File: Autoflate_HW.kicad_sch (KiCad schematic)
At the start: 70 parts, among them J1 JST_XH_3, J10 JST_VH_2, J11 JST_VH_2, J12 JST_XH_3, J13 Header_1, J2 JST_VH_3, J3 JST_XH_2, J4 JST_XH_2, J5 JST_XH_2, J6 JST_XH_2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

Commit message: Added Cap on pressure sensor supply
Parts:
- added C10: 1uF, Capacitor_SMD:C_1206_3216Metric_Pad1.33x1.80mm_HandSolder, symbol Device:C
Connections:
- net +5V: now also C10.1
- net GND: now also C10.2
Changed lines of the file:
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@@
   (junction (at 140.97 38.1) (diameter 0) (color 0 0 0 0)
+  )
+  (junction (at 45.72 146.05) (diameter 0) (color 0 0 0 0)
   )
   (junction (at 99.06 52.07) (diameter 0) (color 0 0 0 0)
@@
     (stroke (width 0) (type default) (color 0 0 0 0))
   )
+  (wire (pts (xy 45.72 146.05) (xy 45.72 144.78))
+    (stroke (width 0) (type default) (color 0 0 0 0))
+  )
   (wire (pts (xy 87.63 72.39) (xy 81.28 72.39))
     (stroke (width 0) (type default) (color 0 0 0 0))
@@
     (stroke (width 0) (type default) (color 0 0 0 0))
   )
-  (wire (pts (xy 45.72 156.21) (xy 45.72 154.94))
+  (wire (pts (xy 45.72 156.21) (xy 45.72 146.05))
     (stroke (width 0) (type default) (color 0 0 0 0))
   )
@@
   )
   (wire (pts (xy 87.63 54.61) (xy 81.28 54.61))
+    (stroke (width 0) (type default) (color 0 0 0 0))
+  )
+  (wire (pts (xy 45.72 146.05) (xy 54.61 146.05))
     (stroke (width 0) (type default) (color 0 0 0 0))
   )
@@
     )
   )
-  (symbol (lib_id "power:+5V") (at 45.72 154.94 0) (unit 1)
-    (in_bom yes) (on_board yes) (fields_autoplaced)
-    (property "Reference" "#PWR0105" (id 0) (at 45.72 158.75 0)
-      (effects (font (size 1.27 1.27)) hide)
-    )
-    (property "Value" "+5V" (id 1) (at 45.72 151.3642 0))
-    (property "Footprint" "" (id 2) (at 45.72 154.94 0)
-      (effects (font (size 1.27 1.27)) hide)
-    )
-    (property "Datasheet" "" (id 3) (at 45.72 154.94 0)
+  (symbol (lib_id "power:+5V") (at 45.72 144.78 0) (unit 1)
+    (in_bom yes) (on_board yes) (fields_autoplaced)
+    (property "Reference" "#PWR0105" (id 0) (at 45.72 148.59 0)
+      (effects (font (size 1.27 1.27)) hide)
+    )
+    (property "Value" "+5V" (id 1) (at 45.72 141.2042 0))
+    (property "Footprint" "" (id 2) (at 45.72 144.78 0)
+      (effects (font (size 1.27 1.27)) hide)
+    )
+    (property "Datasheet" "" (id 3) (at 45.72 144.78 0)
       (effects (font (size 1.27 1.27)) hide)
     )
@@
     (pin "2")
   )
+  (symbol (lib_id "power:GND") (at 54.61 153.67 0) (unit 1)
+    (in_bom yes) (on_board yes)
+    (property "Reference" "#PWR0126" (id 0) (at 54.61 160.02 0)
+      (effects (font (size 1.27 1.27)) hide)
+    )
+    (property "Value" "GND" (id 1) (at 58.42 156.21 0))
+    (property "Footprint" "" (id 2) (at 54.61 153.67 0)
+      (effects (font (size 1.27 1.27)) hide)
+    )
+    (property "Datasheet" "" (id 3) (at 54.61 153.67 0)
+      (effects (font (size 1.27 1.27)) hide)
+    )
+    (pin "1")
+  )
   (symbol (lib_id "Device:C_Polarized_US") (at 125.73 44.45 0) (unit 1)
     (in_bom yes) (on_board yes)
@@
     )
     (pin "1")
+  )
+  (symbol (lib_id "Device:C") (at 54.61 149.86 0) (unit 1)
+    (in_bom yes) (on_board yes) (fields_autoplaced)
+    (property "Reference" "C10" (id 0) (at 57.531 149.0253 0)
+      (effects (font (size 1.27 1.27)) (justify left))
+    )
+    (property "Value" "1uF" (id 1) (at 57.531 151.5622 0)
+      (effects (font (size 1.27 1.27)) (justify left))
+    )
+    (property "Footprint" "Capacitor_SMD:C_1206_3216Metric_Pad1.33x1.80mm_HandSolder" (id 2) (at 55.5752 153.67 0)
+      (effects (font (size 1.27 1.27)) hide)
+    )
+    (property "Datasheet" "~" (id 3) (at 54.61 149.86 0)
+      (effects (font (size 1.27 1.27)) hide)
+    )
+    (pin "1")
+    (pin "2")
   )
   (symbol (lib_id "Device:R") (at 229.87 143.51 90) (unit 1)
@@
       (reference "#PWR0125") (unit 1) (value "GND") (footprint "")
     )
+    (path "/a5583439-f3ce-4044-aa4b-15691ff6bcfb"
+      (reference "#PWR0126") (unit 1) (value "GND") (footprint "")
+    )
     (path "/f71d0b0a-699b-470e-8193-907f94f21c11"
       (reference "#PWR0127") (unit 1) (value "GND") (footprint "")
@@
       (reference "C9") (unit 1) (value "33nF") (footprint "Capacitor_SMD:C_0805_2012Metric_Pad1.18x1.45mm_HandSolder")
     )
+    (path "/e028d976-3098-4bd8-8eba-3e1cb9bf2392"
+      (reference "C10") (unit 1) (value "1uF") (footprint "Capacitor_SMD:C_1206_3216Metric_Pad1.33x1.80mm_HandSolder")
+    )
     (path "/23dcefda-c203-49e7-ab3b-d4962ddc6374"

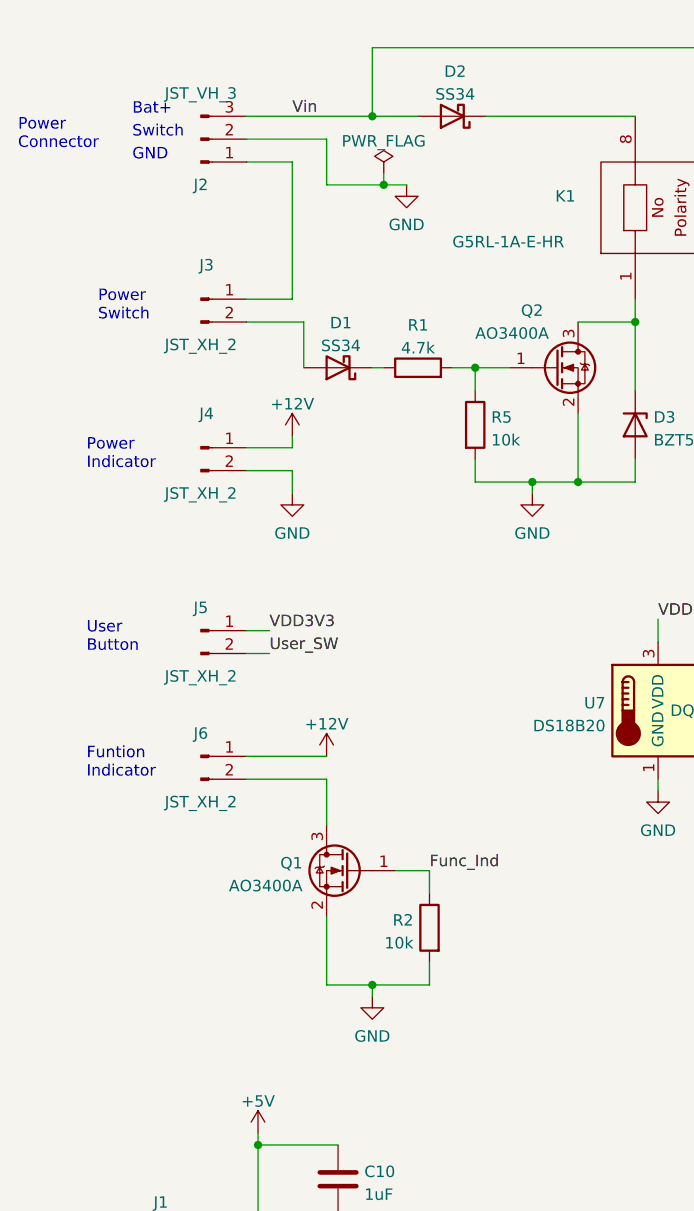
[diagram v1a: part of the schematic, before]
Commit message: 4 pin xh
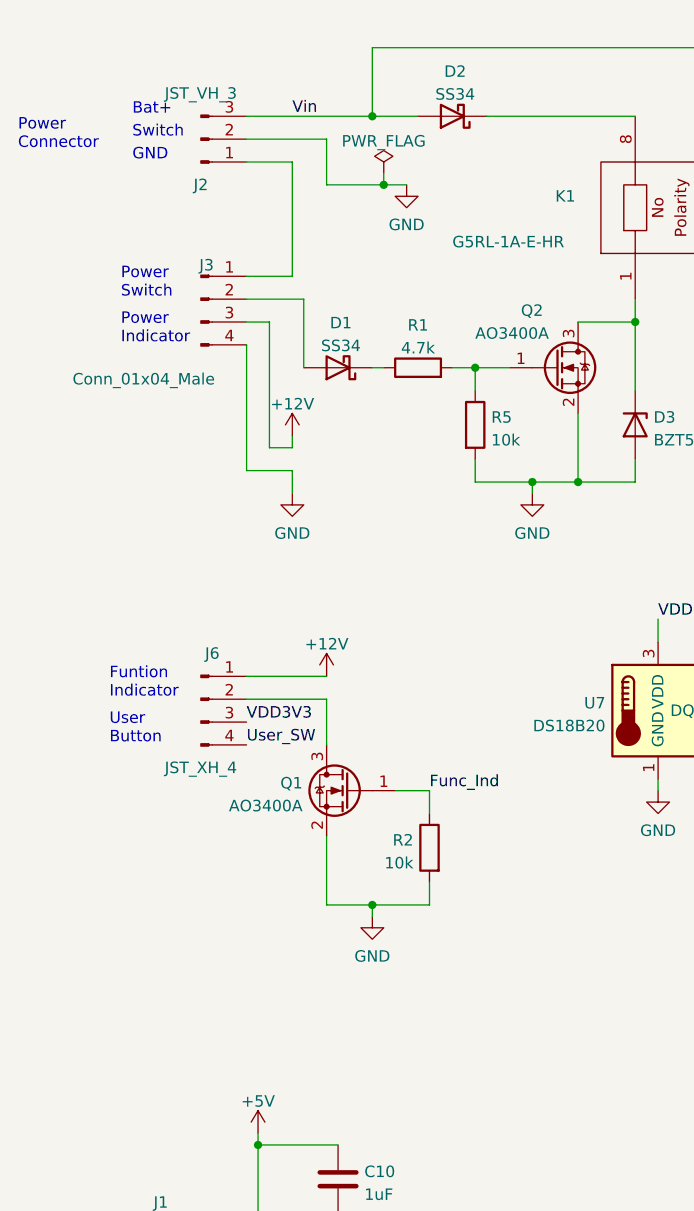
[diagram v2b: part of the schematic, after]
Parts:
- removed J4, J5: JST_XH_2, Connector_JST:JST_XH_B2B-XH-A_1x02_P2.50mm_Vertical, symbol Connector:Conn_01x02_Male
- J3: value JST_XH_2 -> Conn_01x04_Male; footprint Connector_JST:JST_XH_B2B-XH-A_1x02_P2.50mm_Vertical -> Connector_JST:JST_XH_B4B-XH-A_1x04_P2.50mm_Vertical; symbol Connector:Conn_01x02_Male -> Connector:Conn_01x04_Male
- J6: value JST_XH_2 -> JST_XH_4; footprint Connector_JST:JST_XH_B2B-XH-A_1x02_P2.50mm_Vertical -> Connector_JST:JST_XH_B4B-XH-A_1x04_P2.50mm_Vertical; symbol Connector:Conn_01x02_Male -> Connector:Conn_01x04_Male
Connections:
- net +12V: now also J3.3 (Pin_3)
- net GND: now also J3.4 (Pin_4)
- net User_SW: now also J6.4 (Pin_4)
- net VDD3V3: now also J6.3 (Pin_3)
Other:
- moved on the sheet: Q1, R2

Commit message: added buzzer connection
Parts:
- added J4: JST_XH_2, Connector_JST:JST_XH_B2B-XH-A_1x02_P2.50mm_Vertical, symbol Connector:Conn_01x02_Male
- added Q6: AO3400A, Package_TO_SOT_SMD:SOT-23, symbol Transistor_FET:AO3400A
- added R19: 10k, Resistor_SMD:R_0805_2012Metric_Pad1.20x1.40mm_HandSolder, symbol Device:R
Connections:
- net +12V: now also J4.2 (Pin_2)
- net GND: now also Q6.2 (S), R19.2
- net Buzzer: now reaches U3.36 (IO40)
- net Buzzer: now also Q6.1 (G), R19.1
- new net: J4.1 (Pin_1), Q6.3 (D)
- no-connect marks 18 -> 17
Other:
- note added: "Buzzer"
- moved on the sheet: C1, C10, C2, D1, D2, D3, J1, J13, J2, J3, J6, K1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
